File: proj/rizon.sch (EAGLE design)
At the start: 32 parts, among them J1 PWRJACK5521, P1 ADDR, P2 DATA, P3 CTL, P4 PWR, P5 10k, U1 Z8400, U2 AS6C62256PDIP, U3 AS6C62256PDIP, U4 AT28C64BPLCC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

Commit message: Rizon board routing
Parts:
- removed C12: 1uF, dooba:CAP508
- removed C13: 100nF, dooba:CAPDISC
- removed P5: 10k, dooba:PIN_61LINE
- removed U4: AT28C64BPLCC, dooba:AT28C64BPLCC
- removed U6, U8: 7432PDIP, dooba:7432PDIP
- added D1: VCC, dooba:LED5MM
- added D2: VIN, dooba:LED5MM
- added P6: 10k, dooba:PIN_61LINE
- added R1, R2: 1k, dooba:RES8MM
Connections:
- removed net !HIGH_ADDR: U8.2A, U9.1Y
- removed net !MEM_SELECT_LOWRAM: U6.2Y, U8.1A
- removed net !MEM_SELECT_ROM: U6.1Y, U6.3B, U6.4B
- removed net !MEM_SELECT_ROM_BANK0: U6.3Y, U8.3A
- removed net !MEM_SELECT_ROM_BANK1: U6.4Y, U8.4A
- removed net !RAM_BANK1_CE: U3.!CE, U8.2Y
- removed net !ROM_BANK0_CE: U4.!CE, U8.3Y
- removed net !ROM_BANK1: U6.4A, U9.2Y
- removed net !ROM_BANK1_CE: U5.!CE, U8.4Y
- new net !ADDR15: U3.!CE, U9.1Y, U9.3B, U9.4B
- new net !ROM_CE: U5.!CE, U9.3Y
- new net N$1: D2.1, R1.2
- new net N$2: D1.1, R2.2
- net !BUSREQ: now also P3.3, P6.3; no longer P3.2, P5.6
- net !INT: now also P6.2; no longer P5.2
- net !MREQ: no longer U8.1B, U8.2B, U8.3B, U8.4B
- net !NMI: now also P6.1; no longer P5.3
- net !RAM_BANK0_CE: now also U9.4Y; no longer U8.1Y
- net !RD: no longer U4.!OE
- net !RESET: now also P3.4, P6.4; no longer P3.3, P5.5
- net !RFSH: now also P3.2; no longer P3.5
- net !ROM_EN: now also U9.2A, U9.2B, U9.4A; no longer U6.1B, U9.3A, U9.3B
- net !WAIT: now also P3.5, P6.5; no longer P3.4, P5.4
- net !WR: no longer U4.!WE
- net ADDR0: no longer U4.A0
- net ADDR1: no longer U4.A1
- net ADDR10: no longer U4.A10
- net ADDR11: no longer U4.A11
- net ADDR12: no longer U4.A12
- net ADDR13: no longer U6.3A, U9.2A, U9.2B
- net ADDR15: no longer U6.1A, U6.2A
- net ADDR2: no longer U4.A2
- net ADDR3: no longer U4.A3
- net ADDR4: no longer U4.A4
- net ADDR5: no longer U4.A5
- net ADDR6: no longer U4.A6
- net ADDR7: no longer U4.A7
- net ADDR8: no longer U4.A8
- net ADDR9: no longer U4.A9
- net DATA0: no longer U4.I/O0
- net DATA1: no longer U4.I/O1
- net DATA2: no longer U4.I/O2
- net DATA3: no longer U4.I/O3
- net DATA4: no longer U4.I/O4
- net DATA5: no longer U4.I/O5
- net DATA6: no longer U4.I/O6
- net DATA7: no longer U4.I/O7
- net GND: now also D1.2, D2.2; no longer C12.1, C13.1, U4.GND, U6.GND, U8.GND
- net ROM_EN: now also U9.2Y, U9.3A; no longer U6.2B, U9.3Y
- net VCC: now also P6.6, R2.1; no longer C12.2, C13.2, P5.1, U4.VCC, U6.VCC, U8.VCC
- net VIN: now also R1.1
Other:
- note added: "8Kb EEPROM"
- note added: "CPU"
- note added: "Power Supply"
- note removed: "EEPROM 2 x 8Kb"
- note removed: "Memory Device Selector"
- moved on the sheet: C1, C10, C11, C14, C15, C2, C3, C4, C5, C6, C7, C8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

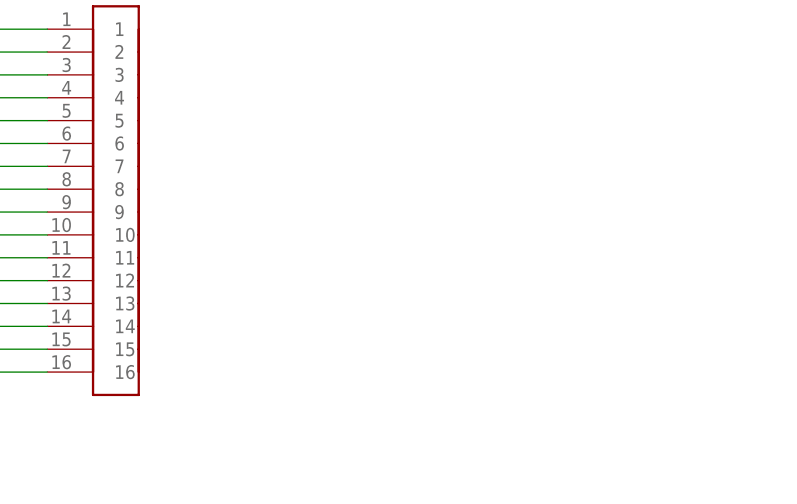
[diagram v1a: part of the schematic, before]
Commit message: Completed Rizon main board (CPU + RAM + ROM) Added Rizon footprint and device to library
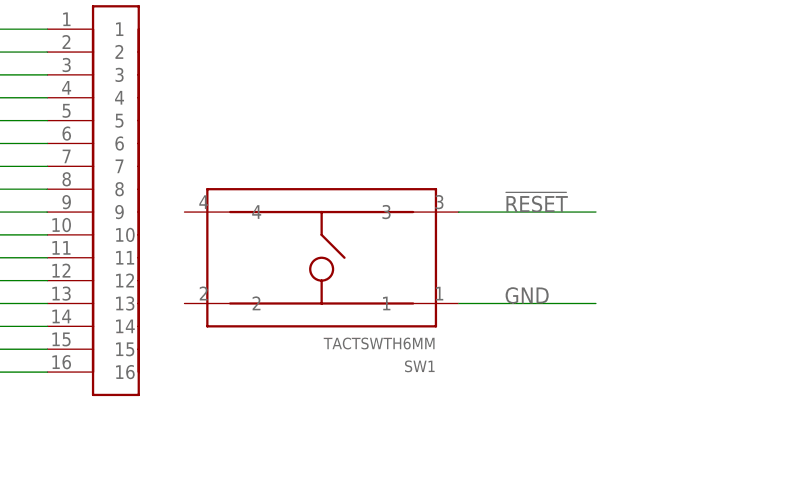
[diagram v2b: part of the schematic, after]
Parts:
- added SW1: TACTSWTH6MM, dooba:TACTSWTH6MM
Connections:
- net !RESET: now also SW1.3
- net GND: now also SW1.1
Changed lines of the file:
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@@
 <?xml version="1.0" encoding="utf-8"?>
 <!DOCTYPE eagle SYSTEM "eagle.dtd">
-<eagle version="8.4.1">
+<eagle version="8.4.0">
 <drawing>
 <settings>
@@
 <part name="R1" library="dooba" deviceset="RES" device="8MM" value="1k"/>
 <part name="R2" library="dooba" deviceset="RES" device="8MM" value="1k"/>
+<part name="SW1" library="dooba" deviceset="TACTSW" device="TH6MM"/>
 </parts>
 <sheets>
@@
 <instance part="R1" gate="R1" x="383.54" y="162.56"/>
 <instance part="R2" gate="R1" x="383.54" y="152.4"/>
+<instance part="SW1" gate="SW1" x="769.62" y="170.18" rot="R180"/>
 </instances>
 <busses>
@@
 <pinref part="GND11" gate="1" pin="GND"/>
 <wire x1="416.56" y1="152.4" x2="419.1" y2="152.4" width="0.1524" layer="91"/>
+</segment>
+<segment>
+<pinref part="SW1" gate="SW1" pin="1"/>
+<wire x1="784.86" y1="165.1" x2="800.1" y2="165.1" width="0.1524" layer="91"/>
+<label x="789.94" y="165.1" size="1.778" layer="95"/>
 </segment>
 </net>
@@
 <label x="716.28" y="187.96" size="1.778" layer="95"/>
 </segment>
-</net>
+<segment>
+<pinref part="SW1" gate="SW1" pin="3"/>
+<wire x1="784.86" y1="175.26" x2="800.1" y2="175.26" width="0.1524" layer="91"/>
+<label x="789.94" y="175.26" size="1.778" layer="95"/>
+</segment>
+</net>

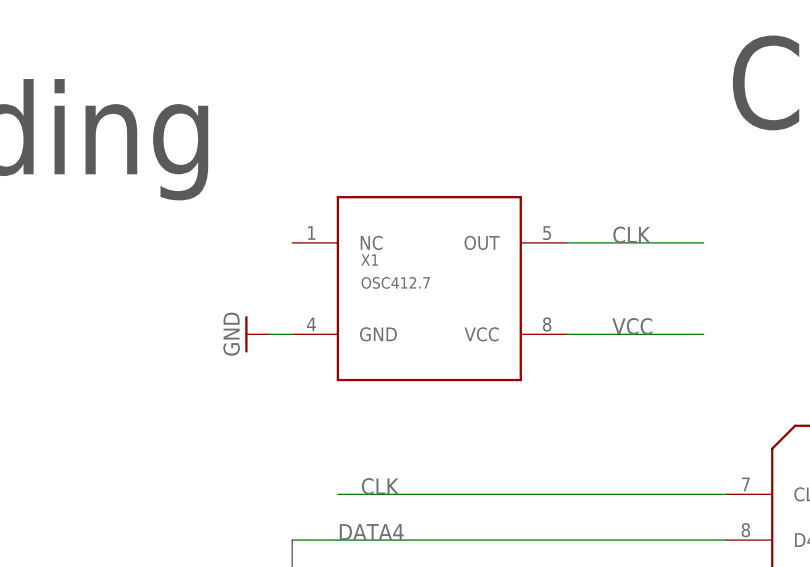
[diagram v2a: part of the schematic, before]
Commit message: Started designing Rizon I/O board schematic
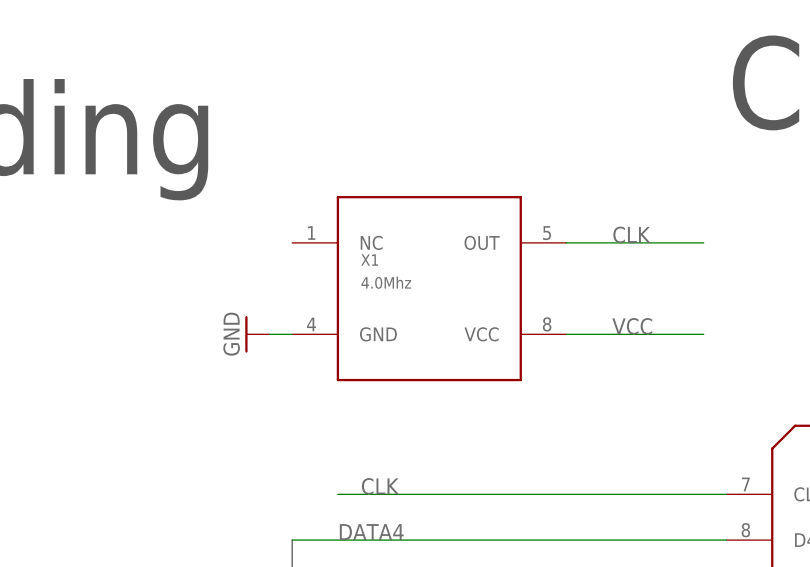
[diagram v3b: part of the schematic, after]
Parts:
- X1: value OSC412.7 -> 4.0Mhz
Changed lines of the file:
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@@
 <?xml version="1.0" encoding="utf-8"?>
 <!DOCTYPE eagle SYSTEM "eagle.dtd">
-<eagle version="8.4.0">
+<eagle version="8.4.1">
 <drawing>
 <settings>
@@
 <part name="U7" library="dooba" deviceset="7805" device="TO220"/>
 <part name="S1" library="dooba" deviceset="SWITCH_SPDT2" device="EG1271"/>
-<part name="X1" library="dooba" deviceset="OSC4" device="12.7"/>
+<part name="X1" library="dooba" deviceset="OSC4" device="12.7" value="4.0Mhz"/>
 <part name="C1" library="dooba" deviceset="CAP_POLARIZED" device="RAD_5MM" value="100uF"/>
 <part name="C2" library="dooba" deviceset="CAP_POLARIZED" device="RAD_5MM" value="10uF"/>
